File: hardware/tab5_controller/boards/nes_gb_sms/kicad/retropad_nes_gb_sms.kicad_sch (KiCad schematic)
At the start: 24 parts, among them J1 Tab5 Ext.Port1, J2 UPDI, SW1 UP, SW2 DOWN, SW3 LEFT, SW4 RIGHT, SW5 1, SW6 2, SW7 START, SW8 MENU, U1 AVR32DD28-I/SO

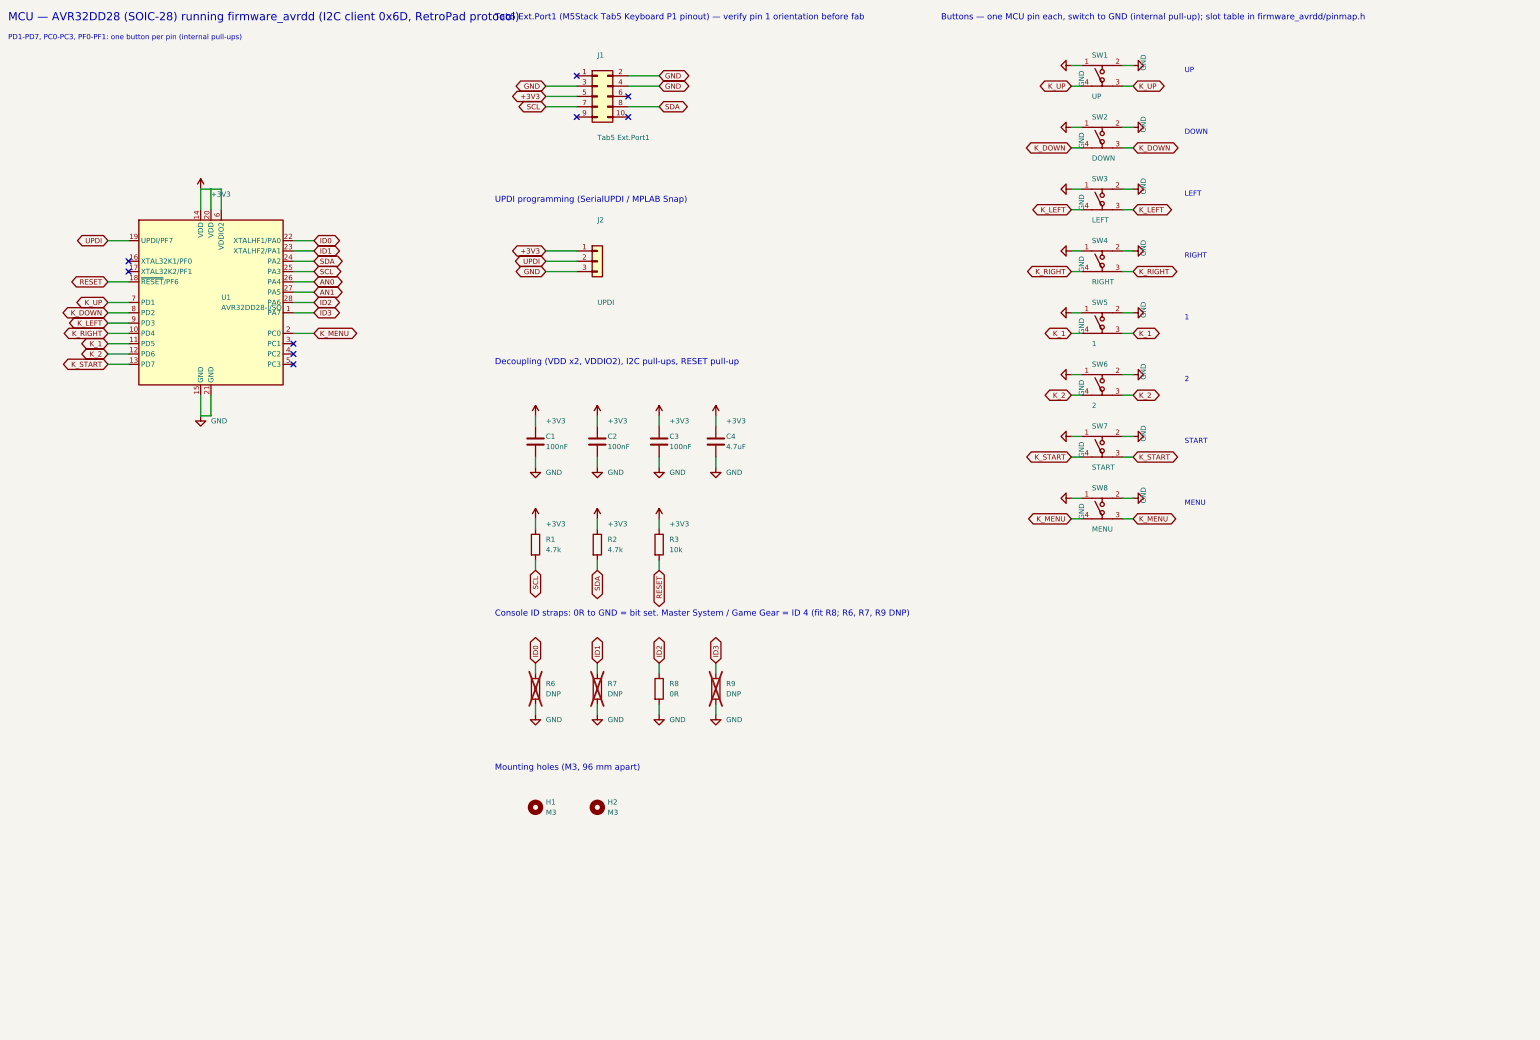
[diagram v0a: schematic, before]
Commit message: tab5_controller: NES / Game Boy / Master System board with a console-select switch
The Master System board had the same controls as the NES / Game Boy one,
so it is merged in: the new nes_gb_sms board picks its console with a
3-position slide switch instead of ID straps.

- Switch: C&K PCM13SMTR (SP3T, right angle, SMD) on the front at the
  bottom edge, lever out through the case wall. Common to GND, positions
  ground ID0 (NES = 1), ID1 (Game Boy = 2) or ID2 (Master System = 4);
  each console is one ID bit, so no logic is needed. Positions are
  labelled in pad order; which lever position closes which pad still
  needs checking against the datasheet (boards/README.md).
- Firmware: the console ID is re-read every 100 ms and a new value takes
  effect after two equal readings, so the switch works while running.
  set_console() keeps SREG intact when called at boot.
- layout.py: ID_SWITCH table; IDs 2 and 4 share the board's slots, so
  the Master System row in pinmap.h now matches the shared board
  (SELECT on PD7, START on PC0, MENU on PC1).
- Board routed: DRC 0 unconnected (silkscreen warnings only), schematic
  vs PCB 0 differences, wiring matches pinmap.h for IDs 1, 2 and 4.
  Host test covers the switch (debounce, passing through a position,
  pull-ups restored) and passes; avr-gcc build 1611 bytes.

Co-Authored-By: Claude Opus 5.5 <noreply@anthropic.com>
Claude-Session: https://claude.ai/code/session_01NhSHTsezreiVZCnuBhQzP2
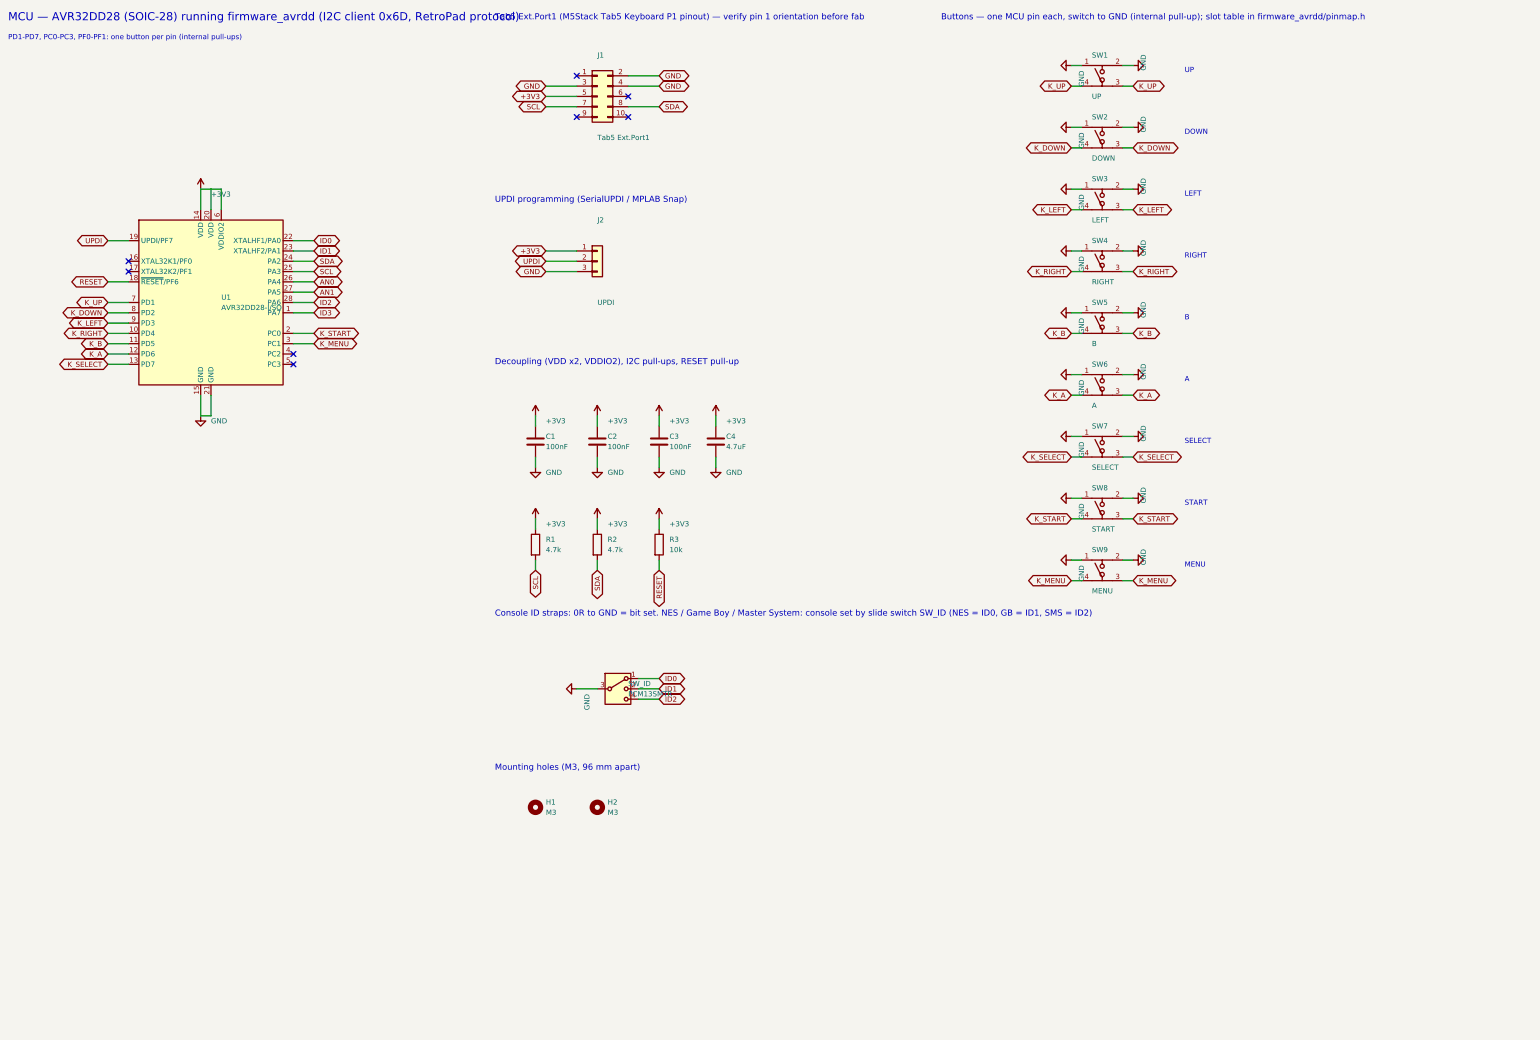
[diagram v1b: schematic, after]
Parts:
- removed R6, R7, R9: DNP, Resistor_SMD:R_0805_2012Metric_Pad1.20x1.40mm_HandSolder, symbol Device:R
- removed R8: 0R, Resistor_SMD:R_0805_2012Metric_Pad1.20x1.40mm_HandSolder, symbol Device:R
- added SW9: MENU, RetroPad:SW_PUSH_6mm_4pin, symbol RetroPad:SW_Push_4pin
- added SW_ID: PCM13SMTR, Button_Switch_SMD:SW_SP3T_PCM13, symbol Switch:SW_SP3T
- SW5: value 1 -> B
- SW6: value 2 -> A
- SW7: value START -> SELECT
- SW8: value MENU -> START
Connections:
- net GND: now also SW9.1, SW9.2, SW_ID.3
- net ID0: now also SW_ID.1
- net ID1: now also SW_ID.2
- net ID2: now also SW_ID.4
- net K_MENU: now also U1.3 (PC1), SW9.3, SW9.4; no longer SW8.3, SW8.4, U1.2 (PC0)
- net K_START: now also SW8.3, SW8.4, U1.2 (PC0); no longer SW7.3, SW7.4, U1.13 (PD7)
- net K_1 renamed K_B
- net K_2 renamed K_A
- new net K_SELECT: SW7.3, SW7.4, U1.13 (PD7)
- no-connect marks 9 -> 8
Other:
- note added: "A"
- note added: "B"
- note added: "Console ID straps: 0R to GND = bit set. NES / Game Boy / Master System: console set by slide switch SW_ID (NES = ID0, GB = ID1, SMS = ID2)"
- note added: "SELECT"
- note removed: "1"
- note removed: "2"
- note removed: "Console ID straps: 0R to GND = bit set. Master System / Game Gear = ID 4 (fit R8; R6, R7, R9 DNP)"
- title: RetroPad Master System / Game Gear controller (console ID 4) -> RetroPad NES / Game Boy / Master System controller (console ID 1)

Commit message: NES/GB/SMS board: CONSOLE button + SK6812MINI-E status LED replace the slide switch
Board (nes_gb_sms):
- ID straps now read 14 (SELECT_STRAP_ID), marking a console-select board
- SW_SEL (6x6 tact, front) on PC3; LED1 SK6812MINI-E reverse-mounted on the
  back through a 3.3 x 2.9 mm cutout, datasheet land pattern, data on PC2 via R10
- LED powered from J1 pin 6 (SYS_EXT5V) through D1 1N4148W (~4.3 V, so the
  3.3 V AVR meets the 0.7*VDD input threshold); C5 decoupling
- Track keepout around the cutout; re-routed: 0 unconnected, no copper-edge
  errors, schematic vs PCB 0 differences

Firmware (FW_VERSION 0x22):
- Select mode: console from EEPROM, each debounced press steps NES -> GB -> SMS,
  saved and shown on the LED (red / green / blue); straps not re-read
- Cycle-counted SK6812 bit-bang on VPORTC.2 (1.25 us per bit at 24 MHz)
- Host test covers select mode with a fake EEPROM

Docs: boards, board, firmware and pin-plan READMEs; BOM parts table.

Co-Authored-By: Claude Opus 5.5 <noreply@anthropic.com>
Claude-Session: https://claude.ai/code/session_01NhSHTsezreiVZCnuBhQzP2
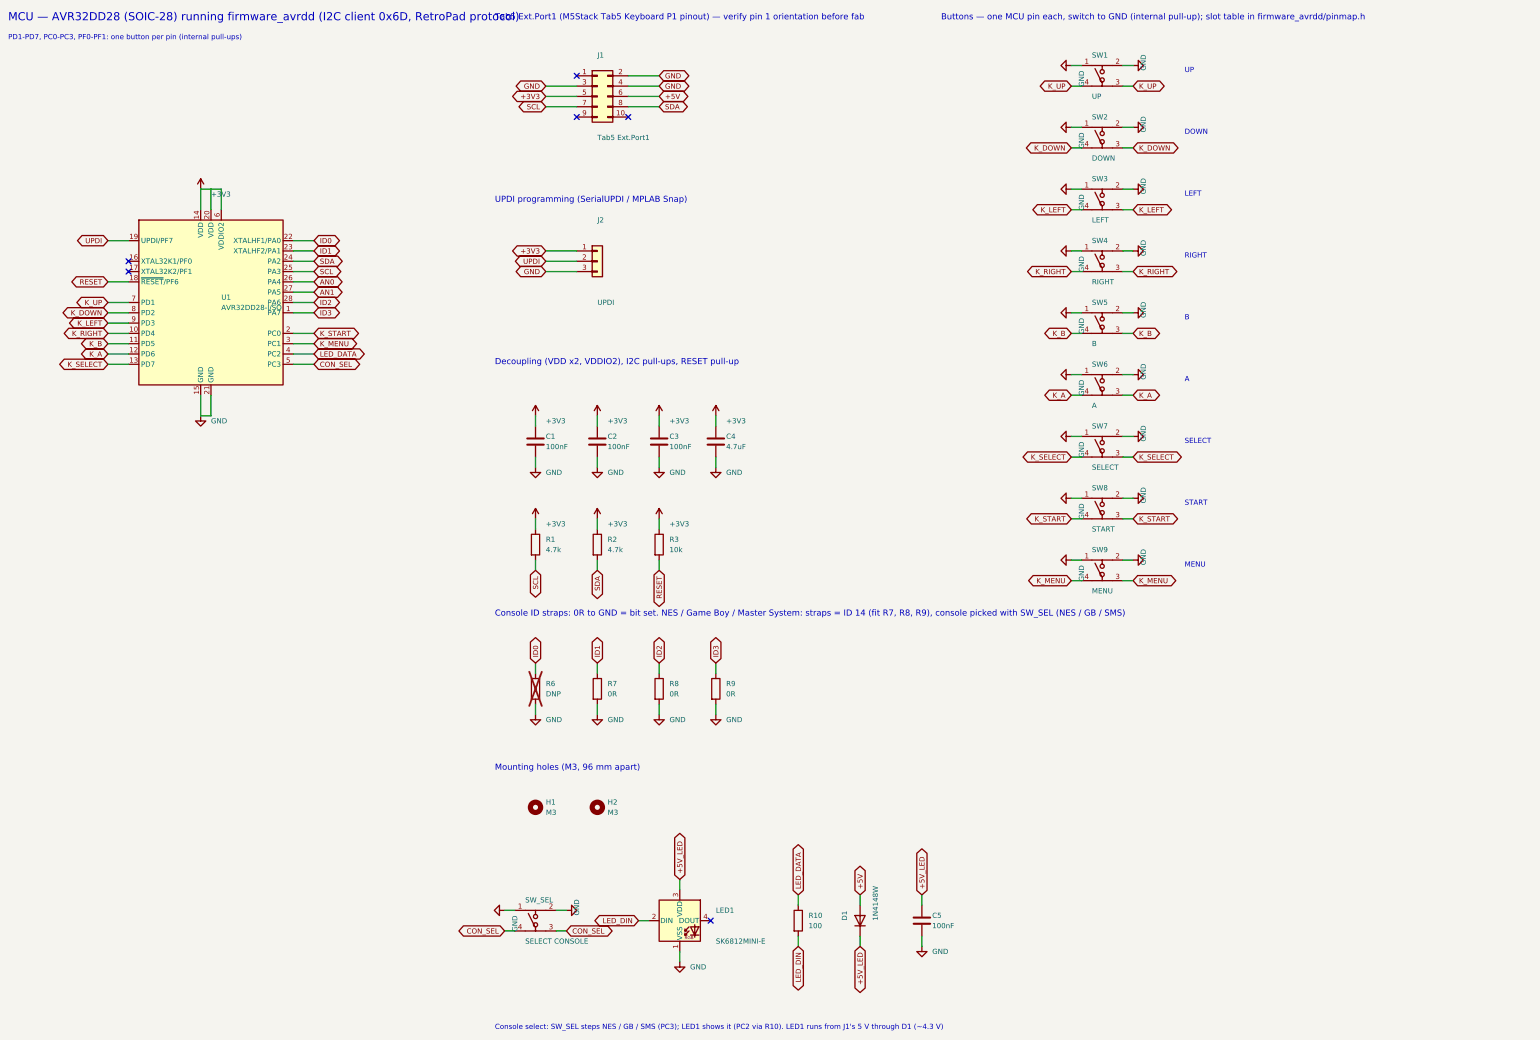
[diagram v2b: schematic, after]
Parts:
- removed SW_ID: PCM13SMTR, Button_Switch_SMD:SW_SP3T_PCM13, symbol Switch:SW_SP3T
- added C5: 100nF, Capacitor_SMD:C_0805_2012Metric_Pad1.18x1.45mm_HandSolder, symbol Device:C
- added D1: 1N4148W, Diode_SMD:D_SOD-123, symbol Device:D
- added LED1: SK6812MINI-E, RetroPad:SK6812MINI-E_ReverseMount, symbol RetroPad:SK6812MINI-E
- added R10: 100, Resistor_SMD:R_0805_2012Metric_Pad1.20x1.40mm_HandSolder, symbol Device:R
- added R6: DNP, Resistor_SMD:R_0805_2012Metric_Pad1.20x1.40mm_HandSolder, symbol Device:R
- added R7, R8, R9: 0R, Resistor_SMD:R_0805_2012Metric_Pad1.20x1.40mm_HandSolder, symbol Device:R
- added SW_SEL: SELECT CONSOLE, RetroPad:SW_PUSH_6mm_4pin, symbol RetroPad:SW_Push_4pin
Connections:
- net GND: now also C5.2, LED1.1 (VSS), R6.2, R7.2, R8.2, R9.2, SW_SEL.1, SW_SEL.2
- net ID0: now also R6.1
- net ID1: now also R7.1
- net ID2: now also R8.1
- net ID3: now also R9.1
- net +5V: now reaches J1.6 (Pin_6)
- net +5V: now also D1.2 (A)
- net LED_DATA: now reaches U1.4 (PC2)
- net LED_DATA: now also R10.1
- net CON_SEL: now reaches U1.5 (PC3)
- net CON_SEL: now also SW_SEL.3, SW_SEL.4
- new net +5V_LED: C5.1, D1.1 (K), LED1.3 (VDD)
- new net LED_DIN: LED1.2 (DIN), R10.2
- no-connect marks 8 -> 6
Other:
- note added: "Console ID straps: 0R to GND = bit set. NES / Game Boy / Master System: straps = ID 14 (fit R7, R8, R9), console picked with SW_SEL (NES / GB / SMS)"
- note added: "Console select: SW_SEL steps NES / GB / SMS (PC3); LED1 shows it (PC2 via R10). LED1 runs from J1's 5 V through D1 (~4.3 V)"
- note removed: "Console ID straps: 0R to GND = bit set. NES / Game Boy / Master System: console set by slide switch SW_ID (NES = ID0, GB = ID1, SMS = ID2)"
- title: RetroPad NES / Game Boy / Master System controller (console ID 1) -> RetroPad NES / Game Boy / Master System controller (console IDs 1/2/4)

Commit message: Board schematics: supplies as global labels so EasyEDA keeps GND / +3V3
EasyEDA's KiCad import names a power symbol's net after its library id, so
GND and +3V3 arrived as power_GND and power_+3V3. gen_sch.py now draws every
supply (GND, +3V3, +5V) as a global label, like the other nets. Netlists are
unchanged: GND, +3V3 (+5V on the NES / GB / SMS board), 0 differences vs PCB.

Also:
- pull-up resistor row offset half a pitch so its +3V3 labels clear the
  decoupling capacitors' GND labels
- shorter schematic title so the NES / GB / SMS one fits the title block
- render.py exported the schematic SVG into the folder that also held
  front/back.svg and globbed the first file, so snes and genesis
  schematic.png showed the PCB back view; the schematic now gets its own folder

Co-Authored-By: Claude Opus 5.5 <noreply@anthropic.com>
Claude-Session: https://claude.ai/code/session_01NhSHTsezreiVZCnuBhQzP2
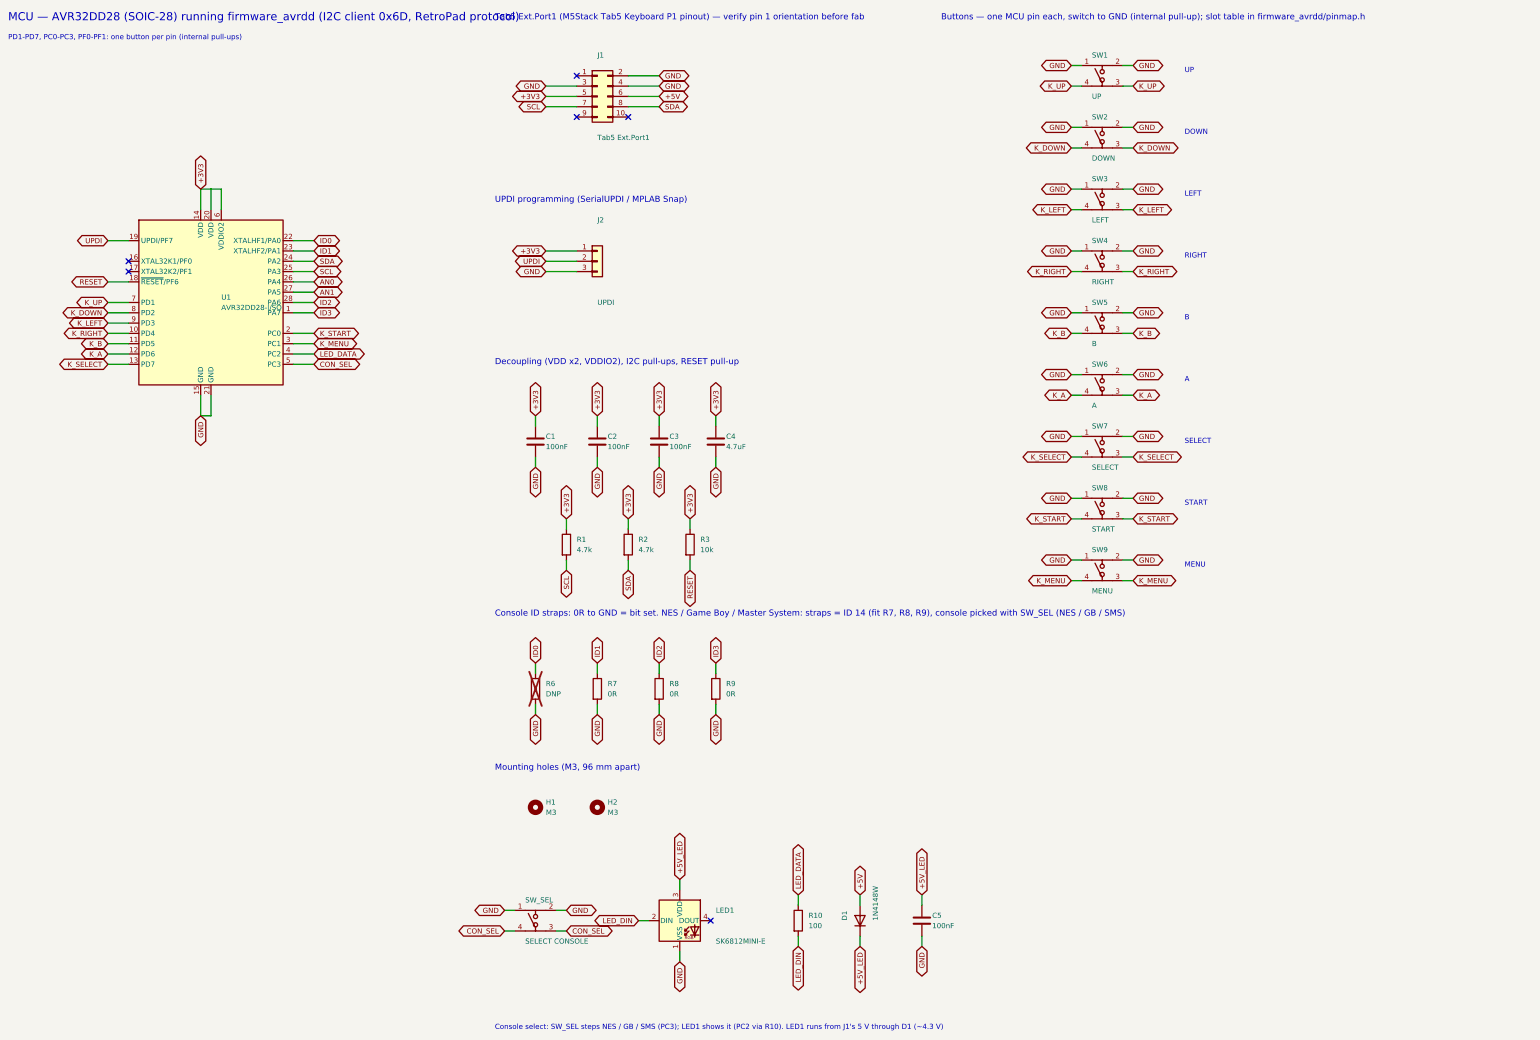
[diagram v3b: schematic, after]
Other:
- title: RetroPad NES / Game Boy / Master System controller (console IDs 1/2/4) -> RetroPad NES / Game Boy / Master System (console IDs 1/2/4)
- moved on the sheet: R1, R2, R3
